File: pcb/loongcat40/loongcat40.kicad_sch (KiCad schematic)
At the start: 83 parts, among them SW1 SW_Push, SW10 SW_Push, SW11 SW_Push, SW12 SW_Push, SW13 SW_Push, SW14 SW_Push, SW15 SW_Push, SW16 SW_Push, SW17 SW_Push, SW18 SW_Push, SW19 SW_Push, SW2 SW_Push, SW20 SW_Push, SW21 SW_Push, SW22 SW_Push, SW23 SW_Push, SW24 SW_Push, SW25 SW_Push, SW26 SW_Push, SW27 SW_Push, SW28 SW_Push, SW29 SW_Push, SW3 SW_Push, SW30 SW_Push, SW31 SW_Push, SW32 SW_Push, SW33 SW_Push, SW34 SW_Push, SW35 SW_Push, SW36 SW_Push, SW37 SW_Push, SW38 SW_Push, SW39 SW_Push, SW4 SW_Push, SW40 SW_Push, SW5 SW_Push, SW6 SW_Push, SW7 SW_Push, SW8 SW_Push, SW9 SW_Push

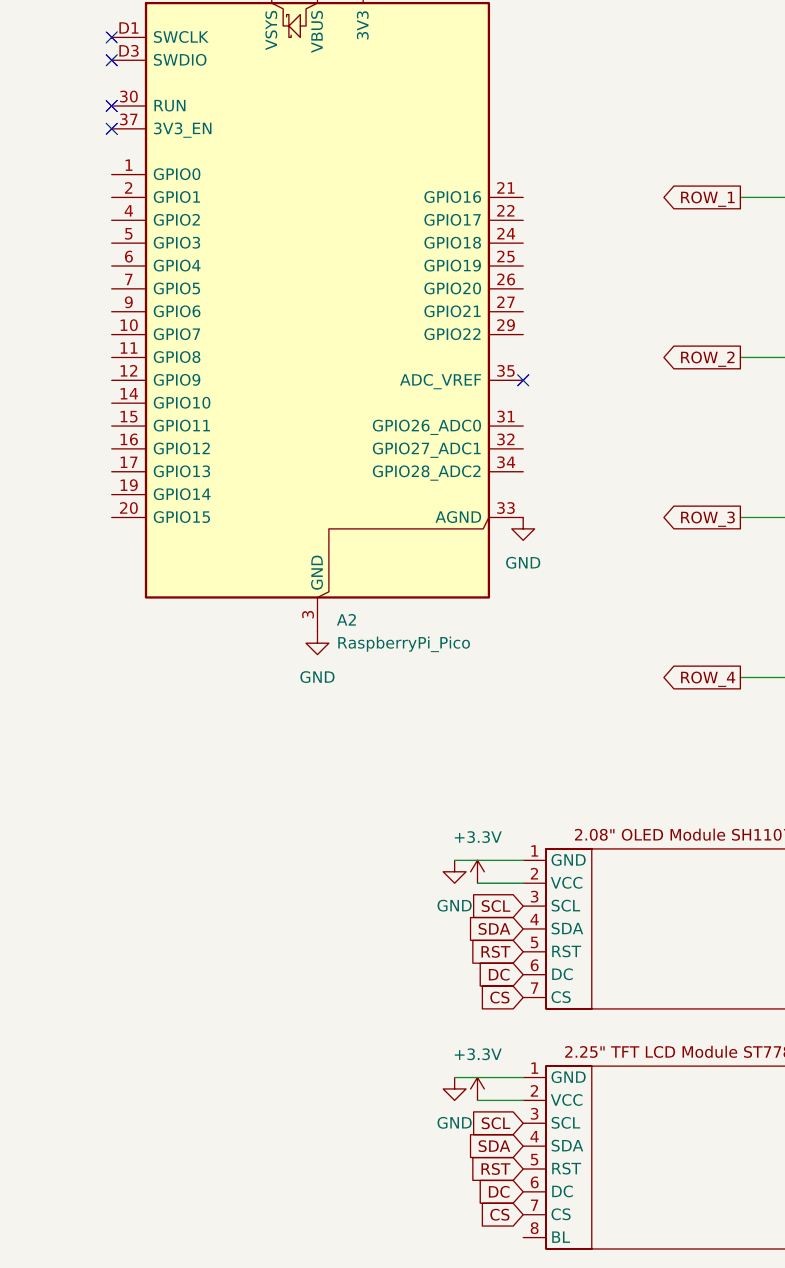
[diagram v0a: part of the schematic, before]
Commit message: position parts on pcb
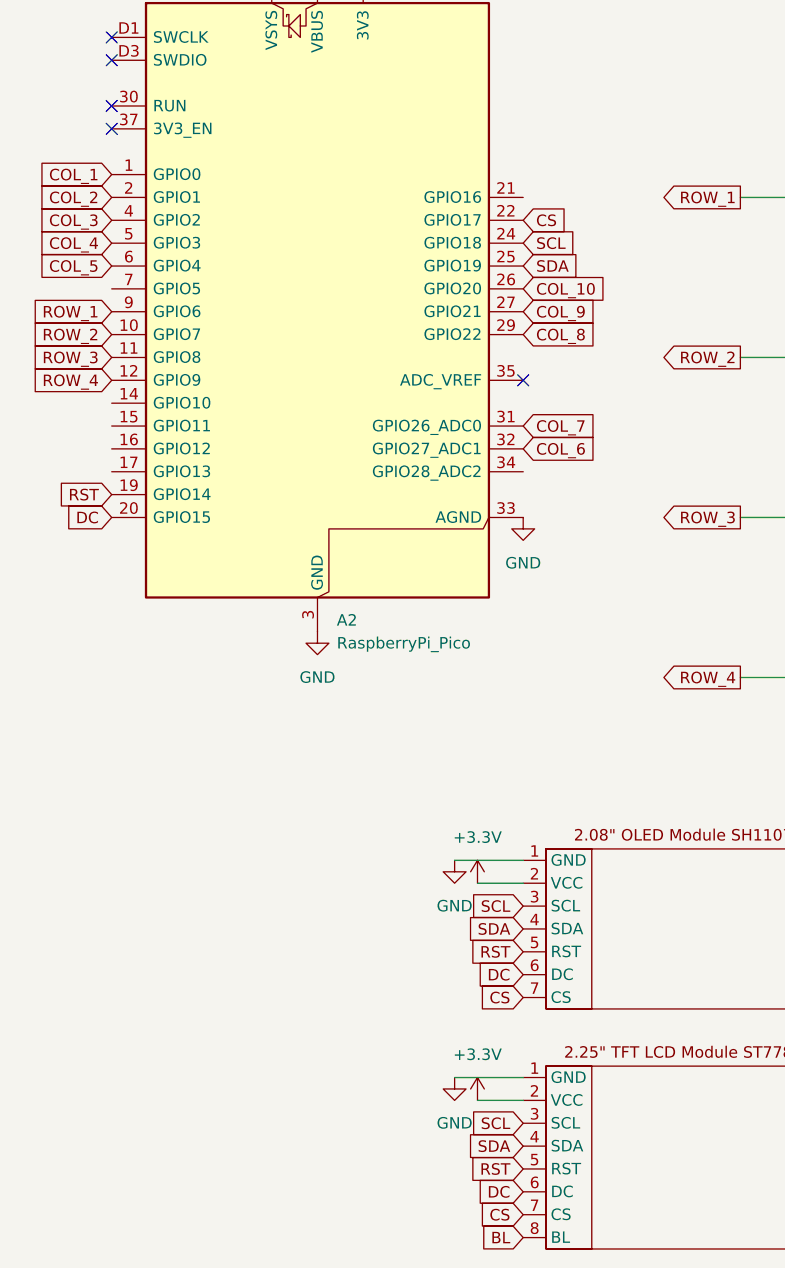
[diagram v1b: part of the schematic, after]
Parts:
- SW1, SW10, SW11, SW12, SW13, SW14, SW15, SW16, SW17, SW18, SW19, SW2, SW20, SW21, SW22, SW23, SW24, SW25, SW26, SW27, SW28, SW29, SW3, SW30, SW31, SW32, SW33, SW34, SW35, SW36, SW37, SW38, SW39, SW4, SW40, SW5, SW6, SW7, SW8, SW9: footprint (none) -> marbastlib-mx:SW_MX_HS_CPG151101S11_1u
- U1: footprint (none) -> local:SH1122_2.08inch
- U2: footprint (none) -> local:ST7789_2.25inch
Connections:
- net COL_1: now also A2.1 (GPIO0)
- net COL_10: now also A2.26 (GPIO20)
- net COL_2: now also A2.2 (GPIO1)
- net COL_3: now also A2.4 (GPIO2)
- net COL_4: now also A2.5 (GPIO3)
- net COL_5: now also A2.6 (GPIO4)
- net COL_6: now also A2.32 (GPIO27_ADC1)
- net COL_7: now also A2.31 (GPIO26_ADC0)
- net COL_8: now also A2.29 (GPIO22)
- net COL_9: now also A2.27 (GPIO21)
- net CS: now also A2.22 (GPIO17)
- net DC: now also A2.20 (GPIO15)
- net ROW_1: now also A2.9 (GPIO6)
- net ROW_2: now also A2.10 (GPIO7)
- net ROW_3: now also A2.11 (GPIO8)
- net ROW_4: now also A2.12 (GPIO9)
- net RST: now also A2.19 (GPIO14)
- net SCL: now also A2.24 (GPIO18)
- net SDA: now also A2.25 (GPIO19)
- net BL: now reaches U2.8 (BL)

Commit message: create outputs; init keyboard case
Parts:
- added H1, H2, H3, H4, H5, H6: MountingHole_Pad, MountingHole:MountingHole_2.2mm_M2_Pad, symbol Mechanical:MountingHole_Pad
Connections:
- net BL: now also A2.17 (GPIO13)
- net GND: now also H1.1, H2.1, H3.1, H4.1, H5.1, H6.1
- no-connect marks 6 -> 12

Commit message: update pcb to v0.1
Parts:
- added SW41, SW42: SW_Push, keyswitches:Kailh_socket_MX, symbol Switch:SW_Push
- A2: footprint Module:RaspberryPi_Pico_SMD_HandSolder -> Module:RaspberryPi_Pico_Common_Unspecified
- SW1, SW10, SW11, SW12, SW13, SW14, SW15, SW16, SW17, SW18, SW19, SW2, SW20, SW21, SW22, SW23, SW24, SW25, SW26, SW27, SW28, SW29, SW3, SW30, SW31, SW32, SW33, SW34, SW35, SW36, SW37, SW38, SW39, SW4, SW40, SW5, SW6, SW7, SW8, SW9: footprint marbastlib-mx:SW_MX_HS_CPG151101S11_1u -> keyswitches:Kailh_socket_MX
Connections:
- net COL_1: now also SW1.1, SW11.1, SW21.1, SW31.1; no longer SW1.2, SW11.2, SW21.2, SW31.2
- net COL_10: now also SW10.1, SW20.1, SW30.1, SW40.1; no longer SW10.2, SW20.2, SW30.2, SW40.2
- net COL_2: now also SW12.1, SW2.1, SW22.1, SW32.1; no longer SW12.2, SW2.2, SW22.2, SW32.2
- net COL_3: now also SW13.1, SW23.1, SW3.1, SW33.1; no longer SW13.2, SW23.2, SW3.2, SW33.2
- net COL_4: now also SW14.1, SW24.1, SW34.1, SW4.1; no longer SW14.2, SW24.2, SW34.2, SW4.2
- net COL_5: now also SW15.1, SW25.1, SW35.1, SW5.1, SW41.1; no longer SW15.2, SW25.2, SW35.2, SW5.2
- net COL_6: now also SW16.1, SW26.1, SW36.1, SW6.1, SW42.1; no longer SW16.2, SW26.2, SW36.2, SW6.2
- net COL_7: now also SW17.1, SW27.1, SW37.1, SW7.1; no longer SW17.2, SW27.2, SW37.2, SW7.2
- net COL_8: now also SW18.1, SW28.1, SW38.1, SW8.1; no longer SW18.2, SW28.2, SW38.2, SW8.2
- net COL_9: now also SW19.1, SW29.1, SW39.1, SW9.1; no longer SW19.2, SW29.2, SW39.2, SW9.2
- net at D11.2 (A): now also SW11.2; no longer SW11.1
- net at D4.2 (A): now also SW4.2; no longer SW4.1
- net at D18.2 (A): now also SW18.2; no longer SW18.1
- net at D35.2 (A): now also SW35.2, SW41.2; no longer SW35.1
- net at D5.2 (A): now also SW5.2; no longer SW5.1
- net at D27.2 (A): now also SW27.2; no longer SW27.1
- net at D6.2 (A): now also SW6.2; no longer SW6.1
- net at D21.2 (A): now also SW21.2; no longer SW21.1
- net at D16.2 (A): now also SW16.2; no longer SW16.1
- net at D10.2 (A): now also SW10.2; no longer SW10.1
- net at D15.2 (A): now also SW15.2; no longer SW15.1
- net at D17.2 (A): now also SW17.2; no longer SW17.1
- net at D9.2 (A): now also SW9.2; no longer SW9.1
- net at D12.2 (A): now also SW12.2; no longer SW12.1
- net at D26.2 (A): now also SW26.2; no longer SW26.1
- net at D1.2 (A): now also SW1.2; no longer SW1.1
- net at D36.2 (A): now also SW36.2, SW42.2; no longer SW36.1
- net at D38.2 (A): now also SW38.2; no longer SW38.1
- net at D24.2 (A): now also SW24.2; no longer SW24.1
- net at D22.2 (A): now also SW22.2; no longer SW22.1
- net at D40.2 (A): now also SW40.2; no longer SW40.1
- net at D8.2 (A): now also SW8.2; no longer SW8.1
- net at D32.2 (A): now also SW32.2; no longer SW32.1
- net at D19.2 (A): now also SW19.2; no longer SW19.1
- net at D34.2 (A): now also SW34.2; no longer SW34.1
- net at D30.2 (A): now also SW30.2; no longer SW30.1
- net at D25.2 (A): now also SW25.2; no longer SW25.1
- net at D2.2 (A): now also SW2.2; no longer SW2.1
- net at D29.2 (A): now also SW29.2; no longer SW29.1
- net at D14.2 (A): now also SW14.2; no longer SW14.1
- net at D28.2 (A): now also SW28.2; no longer SW28.1
- net at D33.2 (A): now also SW33.2; no longer SW33.1
- net at D20.2 (A): now also SW20.2; no longer SW20.1
- net at D7.2 (A): now also SW7.2; no longer SW7.1
- net at D39.2 (A): now also SW39.2; no longer SW39.1
- net at D37.2 (A): now also SW37.2; no longer SW37.1
- net at D31.2 (A): now also SW31.2; no longer SW31.1
- net at D23.2 (A): now also SW23.2; no longer SW23.1
- net at D13.2 (A): now also SW13.2; no longer SW13.1
- net at D3.2 (A): now also SW3.2; no longer SW3.1
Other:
- note added: "switch symbols have been flipped to switch over to new mx footprint"
- moved on the sheet: SW1, SW10, SW11, SW12, SW13, SW14, SW15, SW16, SW17, SW18, SW19, SW2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

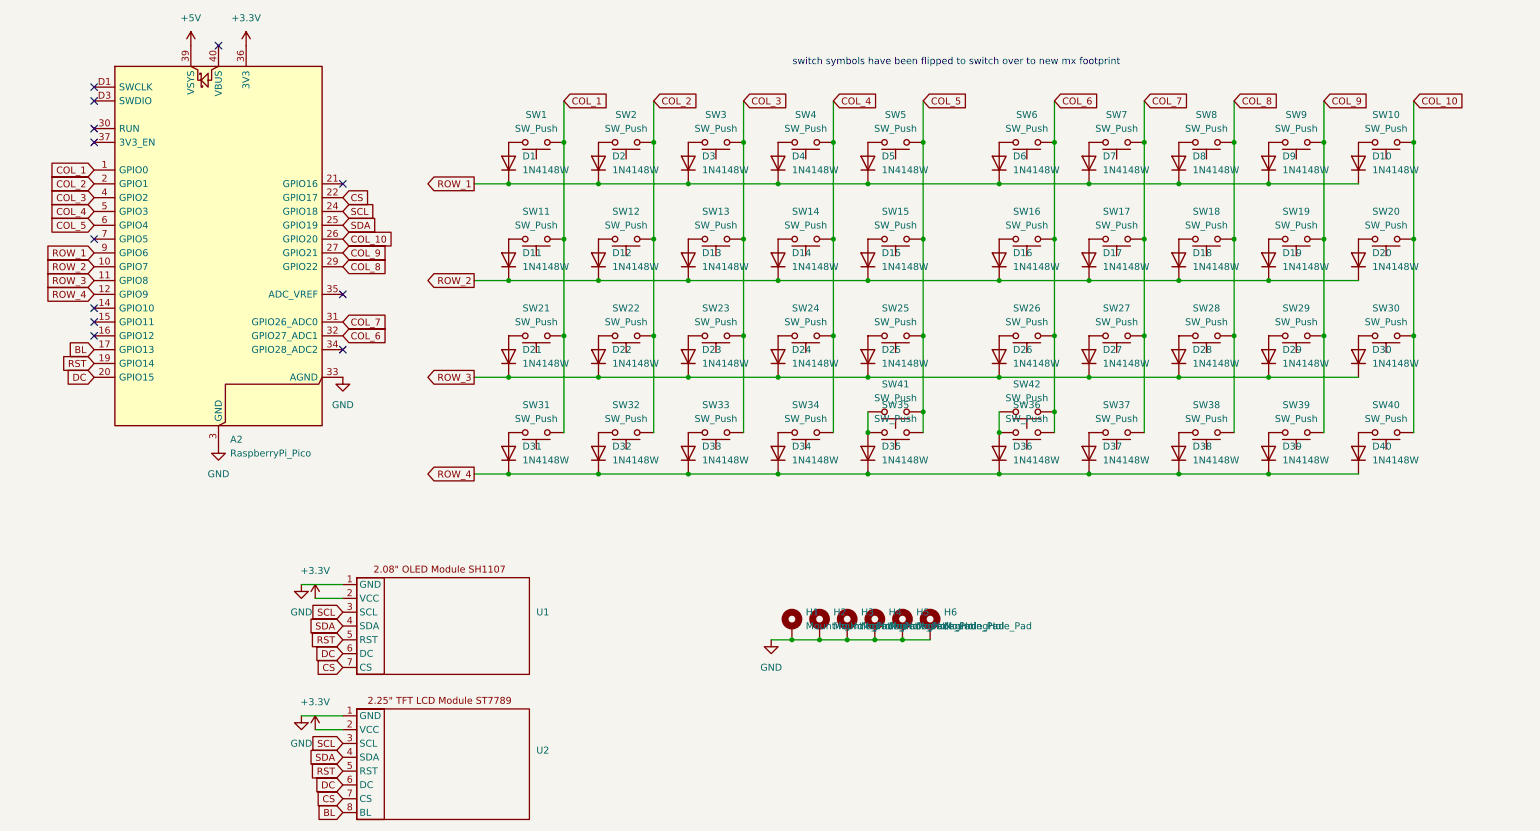
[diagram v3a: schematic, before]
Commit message: update pcb to support 2U stabilizers, update col10 pin
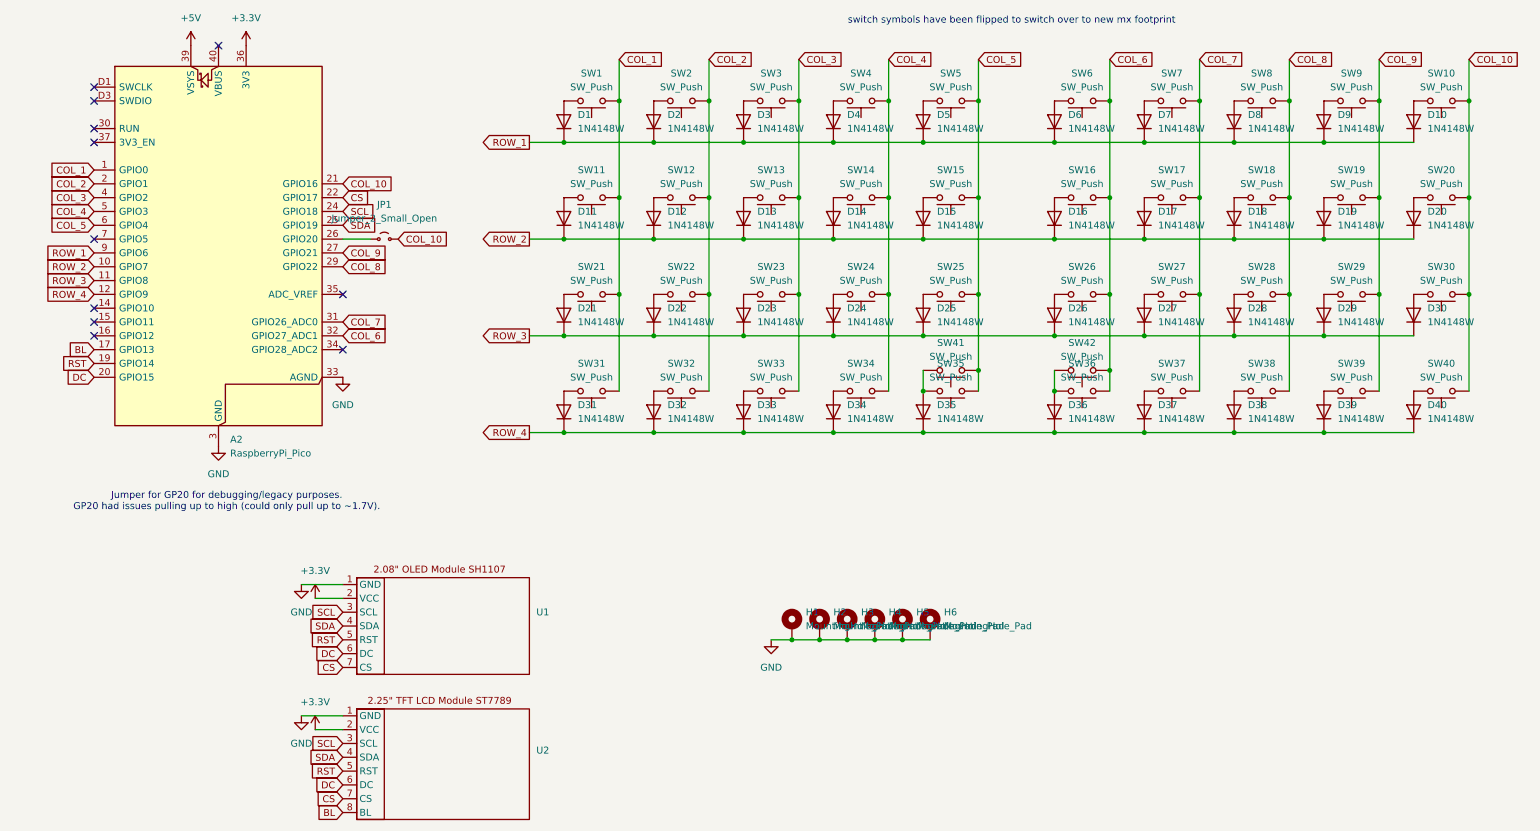
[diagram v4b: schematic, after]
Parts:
- added JP1: Jumper_2_Small_Open, Jumper:SolderJumper-2_P1.3mm_Open_RoundedPad1.0x1.5mm, symbol Jumper:Jumper_2_Small_Open
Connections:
- net COL_10: now also A2.21 (GPIO16), JP1.2 (B); no longer A2.26 (GPIO20)
- new net: A2.26 (GPIO20), JP1.1 (A)
- no-connect marks 12 -> 11
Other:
- note added: "Jumper for GP20 for debugging/legacy purposes. GP20 had issues pulling up to high (could only pull up to ~1.7V)."
- moved on the sheet: D1, D10, D11, D12, D13, D14, D15, D16, D17, D18, D19, D2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
